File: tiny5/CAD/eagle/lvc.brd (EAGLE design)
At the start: 31.8 x 31.8 mm, 28 parts, among them J1 3,5MM_1X2_SCREWTERM, J2 3,5MM_1X2_SCREWTERM, Q1 FDC6312P, Q2 PMGD280UN, Q3 SQJ463EP, U1 LT3007, U2 ATTINY5, U3 LT1494

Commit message: Finished routing
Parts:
- added J3: 2X3_50MIL, NR_conn:50MIL_2X3
- added JP1: (no value), pinhead:1X02
- added R12: 100k, resistor:R0603
- added S2: CL-SB-12B-02, AR_switches:CL-SB-12B
- moved R10 74.2 mm to (13.8, 4.05), turned to 180 degrees
- moved U3 69.2 mm to (22.2, 14.7), turned to 90 degrees
- moved R8 68.9 mm to (13.8, 5.56), turned to 180 degrees
- moved R4 68.5 mm to (25.1, 29.4), turned to 90 degrees
- moved U1 66.4 mm to (15.7, 15.8)
- moved C2 65.4 mm to (16.0, 12.7), turned to 180 degrees
- moved R2 63.5 mm to (22.7, 17.3), turned to 180 degrees
- moved C4 62.3 mm to (6.35, 13.3), turned to 180 degrees
- moved D2 57.8 mm to (24.5, 27.1)
- moved R3 55.8 mm to (23.6, 29.4), turned to 90 degrees
- moved R1 55.0 mm to (21.6, 29.4), turned to 90 degrees
- moved R11 54.9 mm to (29.2, 12.7), turned to 180 degrees
- moved Q1 54.9 mm to (19.1, 29.1)
- moved C1 53.4 mm to (18.5, 15.8), turned to 270 degrees
- moved R9 53.2 mm to (13.8, 2.54)
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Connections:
- net N$6 renamed RA
- new net EN: JP1.2, R12.1, S2.1, U1.1
- net GND: now also J1.1, J3.6, R12.2; no longer J1.2
- net LEDS: now also J3.1
- net LOAD: now also J3.3
- net OUT: now also J1.2; no longer J1.1
- net RST: now also J3.5
- net V+: now also JP1.1, S2.2; no longer U1.1
- net VCC: now also J3.2
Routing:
- net V+: track 0.00 -> 69.2 mm, vias 0 -> 5
- net VCC: track 0.00 -> 59.4 mm, vias 0 -> 2
- net LOAD: track 0.00 -> 59.1 mm, vias 0 -> 3
- net LEDS: track 0.00 -> 40.5 mm, vias 0 -> 3
- net N$5: track 0.00 -> 32.4 mm
- net ADC: track 0.00 -> 20.7 mm, vias 0 -> 2
- net EN: track 0.00 -> 17.6 mm
- net ADJ: track 0.00 -> 14.7 mm
- net V_DIV: track 0.00 -> 14.4 mm
- net N$3: track 0.00 -> 14.0 mm, vias 0 -> 2
- net 3_CELL: track 0.00 -> 12.7 mm
- net RST: track 0.00 -> 12.1 mm, vias 0 -> 1
- net 2_CELL: track 0.00 -> 11.7 mm
- net GND: track 0.00 -> 9.94 mm, vias 0 -> 34
- net N$4: track 0.00 -> 8.90 mm, vias 0 -> 2
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- added copper zone on layer 1, net GND
- added copper zone on layer 16, net GND
- added copper zone on layer 1, net OUT
- added copper zone on layer 16, net OUT
- added copper zone on layer 1, net V+
- added copper zone on layer 16, net V+
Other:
- board text added: "3-30V In 10A Max"
- board text added: "Cutoff On Off"
- board text added: "EXT SW"
- board text added: "GND"
- board text added: "Green Blinking"
- board text added: "IN"
- board text added: "LVC Rev 2"
- board text added: "No Lights"
- board text added: "OFF"
- board text added: "ON"
- board text added: "OUT"
- board text added: "Red Blinking"
- board text added: "SN"
- board text added: "STAT"
- board text added: "TPI"

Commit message: Prettified schematic
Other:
- outline, holes or cut-outs redrawn
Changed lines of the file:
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@@
 <layer number="48" name="Document" color="7" fill="1" visible="yes" active="yes"/>
 <layer number="49" name="Reference" color="7" fill="1" visible="yes" active="yes"/>
-<layer number="51" name="tDocu" color="7" fill="1" visible="no" active="yes"/>
+<layer number="51" name="tDocu" color="13" fill="1" visible="yes" active="yes"/>
 <layer number="52" name="bDocu" color="7" fill="1" visible="no" active="yes"/>
 <layer number="90" name="Modules" color="5" fill="1" visible="yes" active="yes"/>
@@
 <board>
 <plain>
-<wire x1="0" y1="0" x2="31.75" y2="0" width="0" layer="20"/>
-<wire x1="31.75" y1="0" x2="31.75" y2="31.75" width="0" layer="20"/>
-<wire x1="31.75" y1="31.75" x2="0" y2="31.75" width="0" layer="20"/>
-<wire x1="0" y1="31.75" x2="0" y2="0" width="0" layer="20"/>
+<wire x1="1.27" y1="0" x2="30.48" y2="0" width="0" layer="20"/>
+<wire x1="31.75" y1="1.27" x2="31.75" y2="30.48" width="0" layer="20"/>
+<wire x1="30.48" y1="31.75" x2="1.27" y2="31.75" width="0" layer="20"/>
 <hole x="2.54" y="29.21" drill="2.5"/>
 <hole x="29.21" y="29.21" drill="2.5"/>
@@
 <text x="22.06625" y="5.3975" size="1.778" layer="21" font="vector" rot="R270">3S</text>
 <text x="16.98625" y="5.3975" size="1.778" layer="21" font="vector" rot="R270">ADJ</text>
+<wire x1="0" y1="30.48" x2="0" y2="1.27" width="0" layer="20"/>
 <wire x1="22.86" y1="5.715" x2="22.86" y2="6.0325" width="0.254" layer="21"/>
 <wire x1="22.86" y1="6.0325" x2="21.74875" y2="7.14375" width="0.254" layer="21"/>
@@
 <wire x1="19.764375" y1="21.74875" x2="19.764375" y2="28.019375" width="0.254" layer="22"/>
 <wire x1="13.49375" y1="21.74875" x2="19.764375" y2="21.74875" width="0.254" layer="22"/>
-<text x="7.9375" y="22.621875" size="1.27" layer="21" font="vector">GND</text>
-<text x="7.9375" y="19.288125" size="1.27" layer="21" font="vector">OUT</text>
-<text x="20.716875" y="22.70125" size="1.27" layer="21" font="vector">GND</text>
-<text x="22.225" y="19.05" size="1.27" layer="21" font="vector">IN</text>
+<text x="7.858125" y="22.86" size="1.27" layer="21" font="vector">GND</text>
+<text x="7.858125" y="19.288125" size="1.27" layer="21" font="vector">OUT</text>
+<text x="20.716875" y="22.780625" size="1.27" layer="21" font="vector">GND</text>
+<text x="22.225" y="19.3675" size="1.27" layer="21" font="vector">IN</text>
 <text x="10.16" y="26.67" size="1.27" layer="22" font="vector" rot="MR270">3-30V In
 10A Max</text>
@@
 <wire x1="10.556875" y1="26.749375" x2="6.588125" y2="26.749375" width="0.254" layer="22"/>
 <wire x1="6.588125" y1="26.749375" x2="6.588125" y2="17.30375" width="0.254" layer="22"/>
+<wire x1="31.75" y1="1.27" x2="30.48" y2="0" width="0" layer="20" curve="-90"/>
+<wire x1="1.27" y1="0" x2="0" y2="1.27" width="0" layer="20" curve="-90"/>
+<wire x1="0" y1="30.48" x2="1.27" y2="31.75" width="0" layer="20" curve="-90"/>
+<wire x1="30.48" y1="31.75" x2="31.75" y2="30.48" width="0" layer="20" curve="-90"/>
 </plain>
 <attributes>
@@
 <via x="20.32" y="26.431875" extent="1-16" drill="0.381"/>
 <via x="6.111875" y="25.796875" extent="1-16" drill="0.381"/>
-<via x="11.033125" y="22.780625" extent="1-16" drill="0.381"/>
+<via x="11.58875" y="23.256875" extent="1-16" drill="0.381"/>
 <via x="20.081875" y="24.13" extent="1-16" drill="0.381"/>
 <via x="15.160625" y="28.813125" extent="1-16" drill="0.381"/>

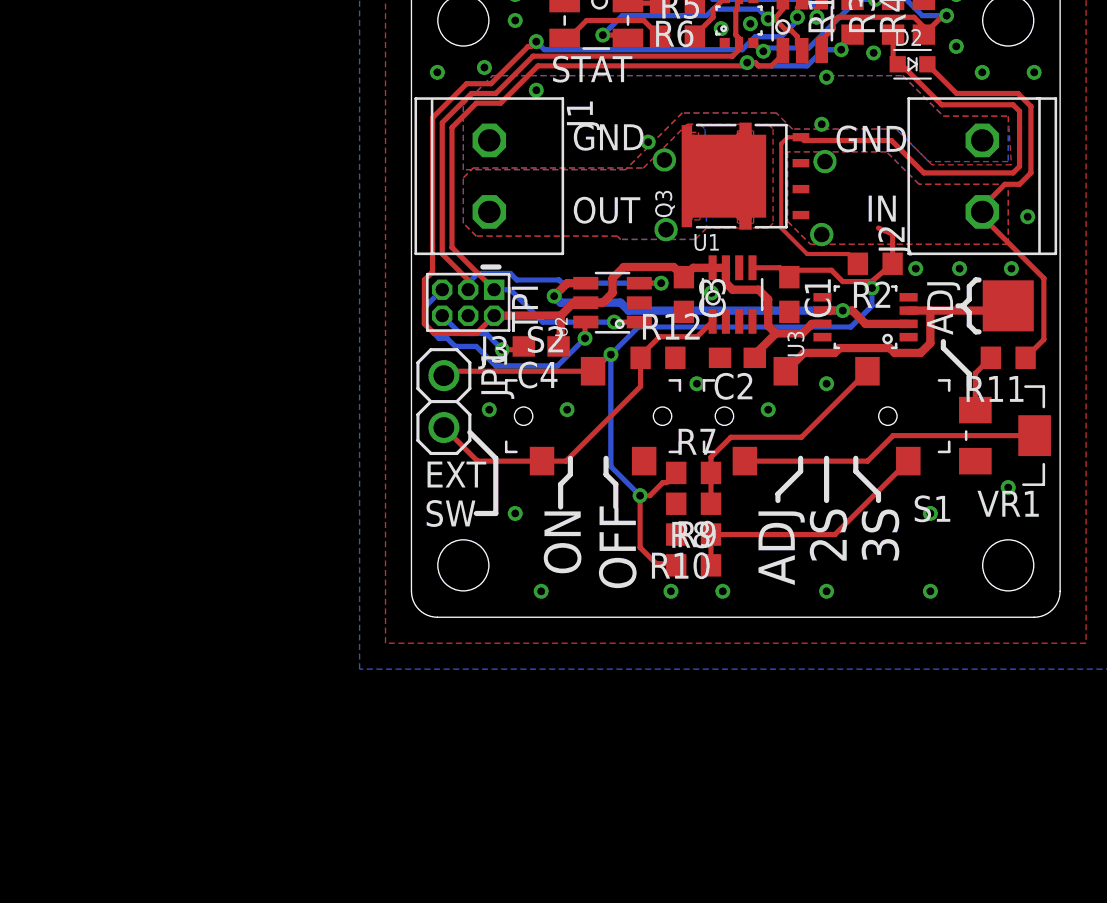
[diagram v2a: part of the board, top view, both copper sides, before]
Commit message: updated schematic for reverse polarity protection
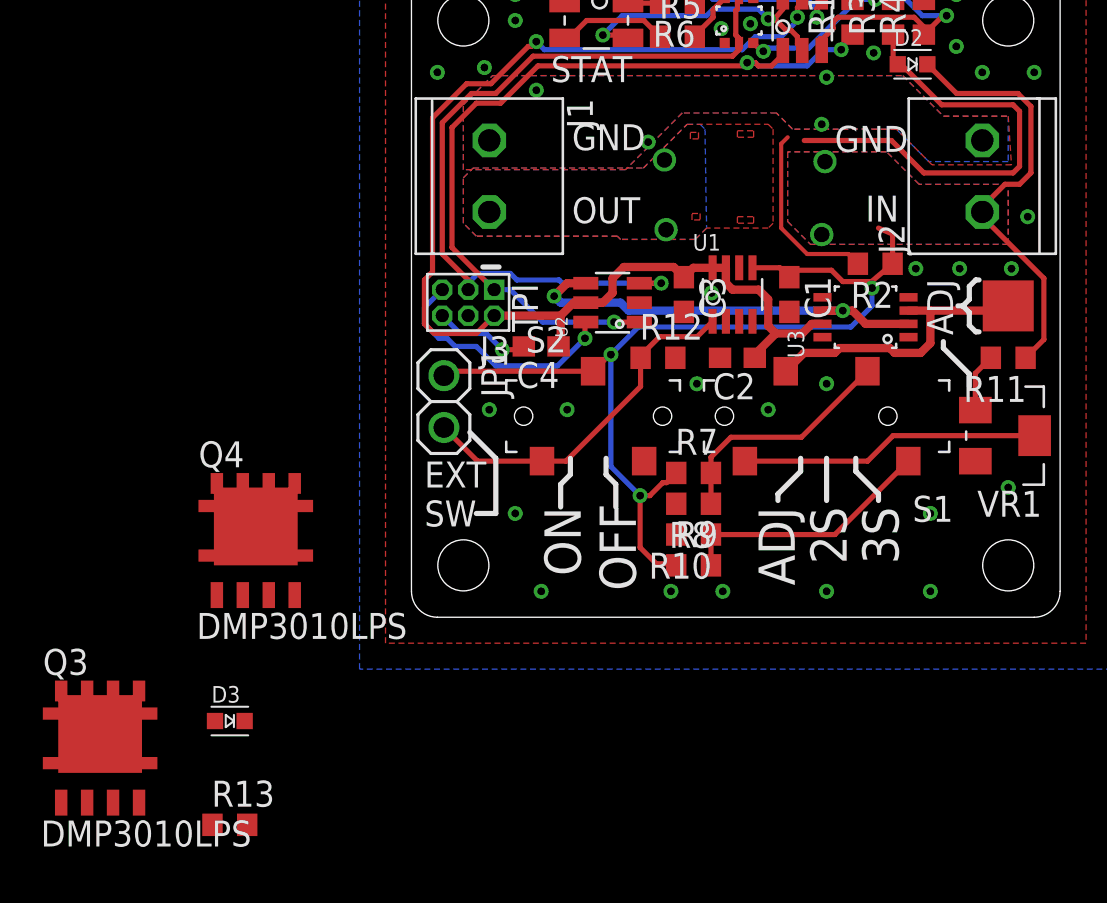
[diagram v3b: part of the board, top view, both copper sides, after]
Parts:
- added D3: MM3Z12VC, NR_diode:SOD-323F
- added Q4: DMP3010LPS, AR_transistor:POWERDI5060-8
- added R13: 1M, resistor:R0603
- Q3: value SQJ463EP -> DMP3010LPS; device AR_transistor:POWERPAK-SO-8L -> AR_transistor:POWERDI5060-8
- R12: value 100k -> 1M
- moved Q3 43.0 mm to (-15.2, -7.62), turned to 0 degrees
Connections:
- new net N$6: D3.1, Q4.G, R13.1
- new net VDD: J2.1, Q4.D1, Q4.D2, Q4.D3, Q4.D4
- net GND: now also R13.2
- net N$5: now also Q3.G; no longer Q3.4
- net OUT: now also Q3.D1, Q3.D2, Q3.D3, Q3.D4; no longer Q3.D, Q3.P$6, Q3.P$7, Q3.P$8
- net V+: now also D3.2, Q3.S1, Q3.S2, Q3.S3, Q4.S1, Q4.S2, Q4.S3; no longer J2.1, Q3.1, Q3.2, Q3.3
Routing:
- net OUT: track 5.32 -> 0.00 mm
- net N$5: track 32.4 -> 31.5 mm

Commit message: yet another transistor (P-FET) update
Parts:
- removed Q4: DMP3010LPS, AR_transistor:POWERDI5060-8
- Q3: value DMP3010LPS -> SI7997DP; device AR_transistor:POWERDI5060-8 -> AR_transistor:POWERPAK-SO-8-DUAL
- moved Q3 8.98 mm to (-24.1, -6.35)
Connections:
- net N$5: now also Q3.2; no longer Q3.G
- net N$6: now also Q3.4; no longer Q4.G
- net OUT: now also Q3.7, Q3.8; no longer Q3.D1, Q3.D2, Q3.D3, Q3.D4
- net V+: now also Q3.1, Q3.3; no longer Q3.S1, Q3.S2, Q3.S3, Q4.S1, Q4.S2, Q4.S3
- net VDD: now also Q3.5, Q3.6; no longer Q4.D1, Q4.D2, Q4.D3, Q4.D4
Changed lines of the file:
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@@
 <element name="S2" library="AR_switches" package="CL-SB-12B" value="CL-SB-12B-02" x="8.89" y="9.8425"/>
 <element name="JP1" library="pinhead" package="1X02" value="" x="1.5875" y="10.556875" rot="R270"/>
-<element name="Q4" library="AR_transistor" package="POWERDI5060-8" value="DMP3010LPS" x="-7.62" y="2.54"/>
 <element name="D3" library="NR_diode" package="SOD-323F" value="MM3Z12VC" x="-8.89" y="-5.08"/>
 <element name="R13" library="resistor" package="R0603" value="1M" x="-8.89" y="-10.16"/>
-<element name="Q3" library="AR_transistor" package="POWERDI5060-8" value="DMP3010LPS" x="-15.24" y="-7.62"/>
+<element name="Q3" library="AR_transistor" package="POWERPAK-SO-8-DUAL" value="SI7997DP" x="-24.13" y="-6.35"/>
 </elements>
 <signals>
@@
 <wire x1="22.5425" y1="16.113125" x2="22.519375" y2="16.13625" width="0.254" layer="1"/>
 <wire x1="22.519375" y1="16.13625" x2="22.519375" y2="16.430625" width="0.254" layer="1"/>
-<contactref element="Q4" pad="S1"/>
-<contactref element="Q4" pad="S2"/>
-<contactref element="Q4" pad="S3"/>
 <contactref element="D3" pad="2"/>
-<contactref element="Q3" pad="S1"/>
-<contactref element="Q3" pad="S2"/>
-<contactref element="Q3" pad="S3"/>
+<contactref element="Q3" pad="3"/>
+<contactref element="Q3" pad="1"/>
 <wire x1="27.94" y1="19.605625" x2="27.94" y2="20.081875" width="0" layer="19" extent="1-1"/>
 <wire x1="23.55125" y1="18.755625" x2="27.94" y2="19.605625" width="0" layer="19" extent="1-1"/>
 <wire x1="20.081875" y1="18.7325" x2="20.558125" y2="16.98625" width="0" layer="19" extent="1-1"/>
 <wire x1="20.240625" y1="22.304375" x2="20.081875" y2="18.7325" width="0" layer="19" extent="1-1"/>
-<wire x1="-6.985" y1="1.085" x2="1.5875" y2="11.826875" width="0" layer="19" extent="1-1"/>
-<wire x1="-8.255" y1="1.085" x2="-6.985" y2="1.085" width="0" layer="19" extent="1-1"/>
-<wire x1="-9.525" y1="1.085" x2="-8.255" y2="1.085" width="0" layer="19" extent="1-1"/>
-<wire x1="-8.165" y1="-5.08" x2="-8.255" y2="1.085" width="0" layer="19" extent="1-1"/>
-<wire x1="-14.605" y1="-9.075" x2="-8.165" y2="-5.08" width="0" layer="19" extent="1-1"/>
-<wire x1="-15.875" y1="-9.075" x2="-14.605" y2="-9.075" width="0" layer="19" extent="1-1"/>
-<wire x1="-17.145" y1="-9.075" x2="-15.875" y2="-9.075" width="0" layer="19" extent="1-1"/>
+<wire x1="-8.165" y1="-5.08" x2="1.5875" y2="11.826875" width="0" layer="19" extent="1-1"/>
+<wire x1="-23.495" y1="-9.075" x2="-8.165" y2="-5.08" width="0" layer="19" extent="1-1"/>
+<wire x1="-26.035" y1="-9.075" x2="-23.495" y2="-9.075" width="0" layer="19" extent="1-1"/>
 </signal>
 <signal name="VCC">
@@
 <wire x1="18.0975" y1="19.05" x2="18.0975" y2="23.1775" width="0.2032" layer="1"/>
 <wire x1="18.0975" y1="23.1775" x2="18.415" y2="23.495" width="0.2032" layer="1"/>
-<contactref element="Q3" pad="G"/>
+<contactref element="Q3" pad="2"/>
 <wire x1="18.415" y1="23.495" x2="19.225" y2="23.33625" width="0" layer="19" extent="1-1"/>
-<wire x1="-13.335" y1="-9.075" x2="18.0975" y2="19.05" width="0" layer="19" extent="1-1"/>
+<wire x1="-24.765" y1="-9.075" x2="18.0975" y2="19.05" width="0" layer="19" extent="1-1"/>
 </signal>
 <signal name="N$7">
@@
 <via x="12.461875" y="18.970625" extent="1-16" drill="0.762"/>
 <via x="12.3825" y="22.38375" extent="1-16" drill="0.762"/>
-<contactref element="Q3" pad="D2"/>
-<contactref element="Q3" pad="D1"/>
-<contactref element="Q3" pad="D3"/>
-<contactref element="Q3" pad="D4"/>
+<contactref element="Q3" pad="7"/>
+<contactref element="Q3" pad="8"/>
 <wire x1="12.461875" y1="18.970625" x2="12.3825" y2="22.38375" width="0" layer="19" extent="1-1"/>
 <wire x1="3.81" y1="19.84" x2="12.461875" y2="18.970625" width="0" layer="19" extent="1-1"/>
-<wire x1="-13.34" y1="-3.42" x2="3.81" y2="19.84" width="0" layer="19" extent="1-1"/>
-<wire x1="-14.59" y1="-3.42" x2="-13.34" y2="-3.42" width="0" layer="19" extent="1-1"/>
-<wire x1="-15.89" y1="-3.42" x2="-14.59" y2="-3.42" width="0" layer="19" extent="1-1"/>
-<wire x1="-17.14" y1="-3.42" x2="-15.89" y2="-3.42" width="0" layer="19" extent="1-1"/>
+<wire x1="-24.73" y1="-3.47" x2="3.81" y2="19.84" width="0" layer="19" extent="1-1"/>
+<wire x1="-26.03" y1="-3.47" x2="-24.73" y2="-3.47" width="0" layer="19" extent="1-1"/>
 </signal>
 <signal name="N$4">
@@
 <signal name="VDD">
 <contactref element="J2" pad="1"/>
-<contactref element="Q4" pad="D2"/>
-<contactref element="Q4" pad="D1"/>
-<contactref element="Q4" pad="D3"/>
-<contactref element="Q4" pad="D4"/>
-<wire x1="-5.72" y1="6.74" x2="27.94" y2="19.84" width="0" layer="19" extent="1-1"/>
-<wire x1="-6.97" y1="6.74" x2="-5.72" y2="6.74" width="0" layer="19" extent="1-1"/>
-<wire x1="-8.27" y1="6.74" x2="-6.97" y2="6.74" width="0" layer="19" extent="1-1"/>
-<wire x1="-9.52" y1="6.74" x2="-8.27" y2="6.74" width="0" layer="19" extent="1-1"/>
+<contactref element="Q3" pad="5"/>
+<contactref element="Q3" pad="6"/>
+<wire x1="-22.23" y1="-3.47" x2="27.94" y2="19.84" width="0" layer="19" extent="1-1"/>
+<wire x1="-23.53" y1="-3.42" x2="-22.23" y2="-3.47" width="0" layer="19" extent="1-1"/>
 </signal>
 <signal name="N$6">
 <contactref element="D3" pad="1"/>
-<contactref element="Q4" pad="G"/>
 <contactref element="R13" pad="1"/>
+<contactref element="Q3" pad="4"/>
+<wire x1="-9.74" y1="-10.16" x2="-22.225" y2="-9.075" width="0" layer="19" extent="1-1"/>
 <wire x1="-9.615" y1="-5.08" x2="-9.74" y2="-10.16" width="0" layer="19" extent="1-1"/>
-<wire x1="-5.715" y1="1.085" x2="-9.615" y2="-5.08" width="0" layer="19" extent="1-1"/>
 </signal>
 </signals>

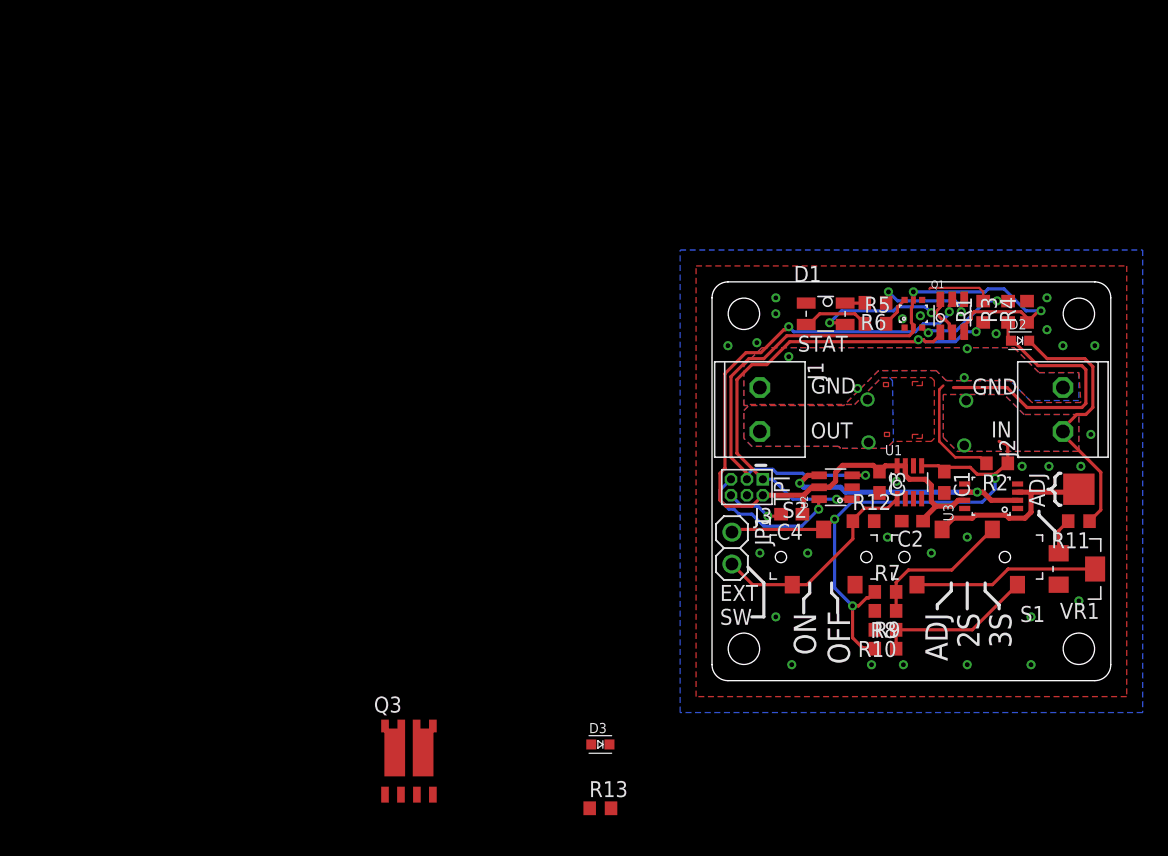
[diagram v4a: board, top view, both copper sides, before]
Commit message: Routed new transistor. Cleaned up transistor package definition
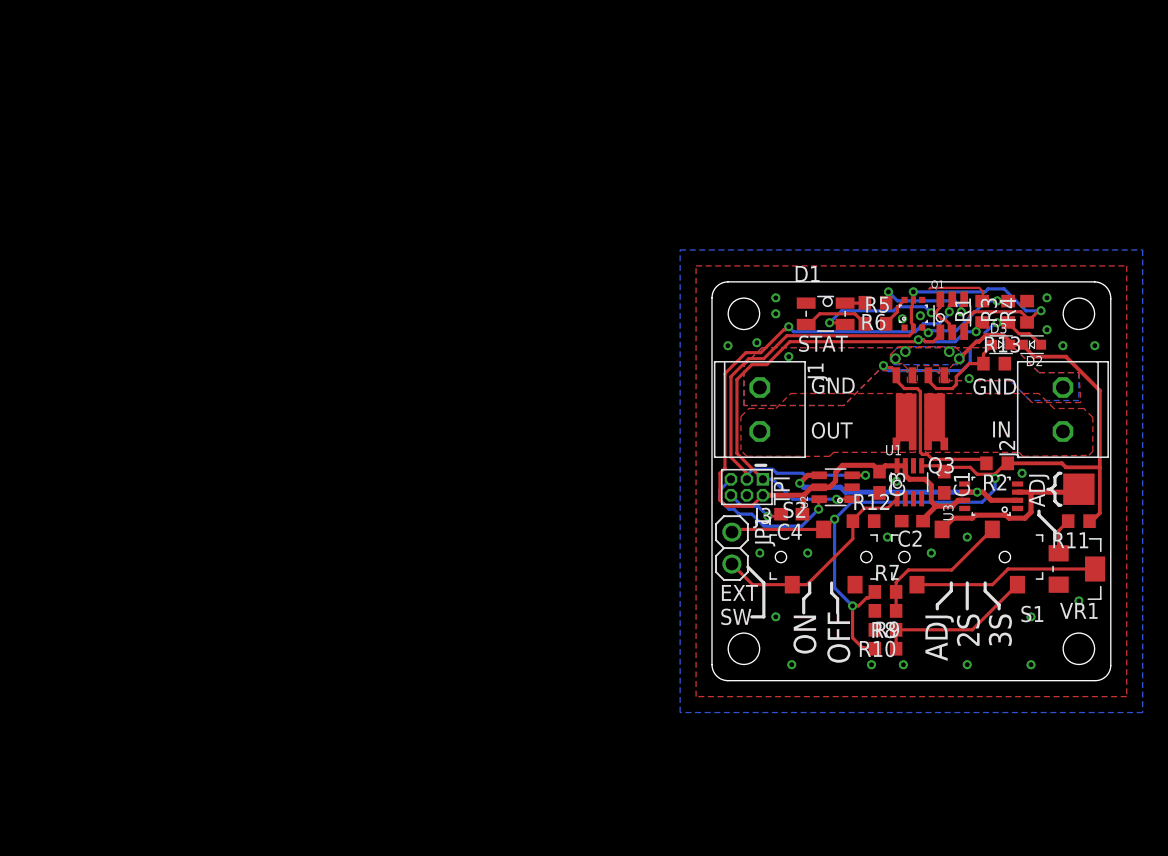
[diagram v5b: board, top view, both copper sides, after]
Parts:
- moved Q3 49.4 mm to (16.6, 21.6), turned to 180 degrees
- moved R13 47.3 mm to (22.5, 25.2)
- moved D3 45.1 mm to (23.0, 26.7)
- moved D2 1.00 mm to (25.5, 26.7), turned to 180 degrees
- moved R1 0.08 mm to (21.5, 29.4)
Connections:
- net N$5: now also Q3.4; no longer Q3.2
- net N$6: now also Q3.2; no longer Q3.4
- net OUT: now also Q3.5, Q3.5L, Q3.6; no longer Q3.7, Q3.8
- net VDD: now also Q3.7, Q3.8, Q3.8L; no longer Q3.5, Q3.6
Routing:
- net V+: track 68.7 -> 78.0 mm, vias 5 -> 7
- net N$6: track 0.00 -> 8.04 mm
- net N$5: track 31.5 -> 30.5 mm, vias 0 -> 2
- net GND: vias 34 -> 28
- added copper zone on layer 1, net VDD
- removed copper zone on layer 16, net OUT
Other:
- outline, holes or cut-outs redrawn
- board text added: "2oz Copper FR-4 or 408 1.0±0.1 Via plate thickness"
